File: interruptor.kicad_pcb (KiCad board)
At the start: 2 copper layers, 23 parts, among them J1 220v, J2 tx/rx, J3 Screw_Terminal_01x03, J4 Screw_Terminal_01x03, J5 Int_1, J6 int_2, J7 switch, K1 SRD-05VDC-SL-C, K2 SRD-05VDC-SL-C, Q1 PN2222A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

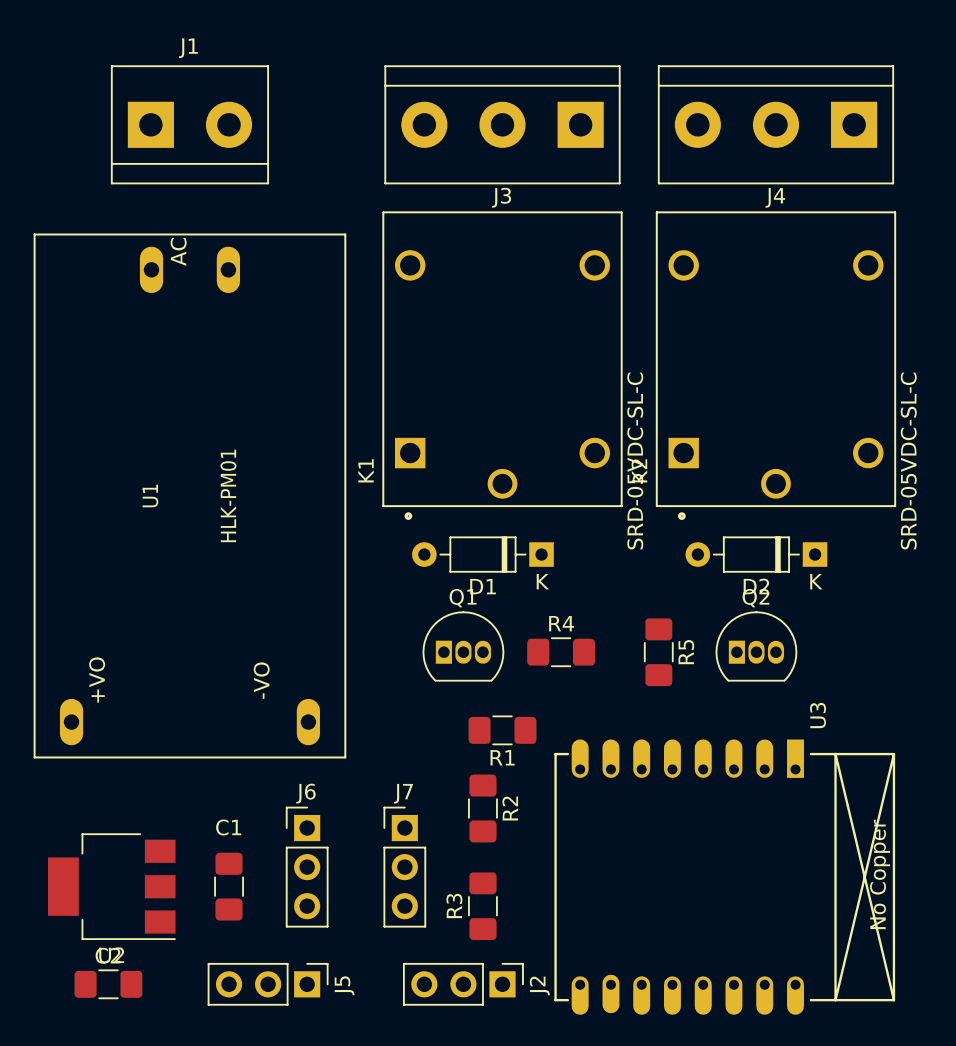
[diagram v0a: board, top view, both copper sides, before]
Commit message: colocacion componentes en pcb y conexionado
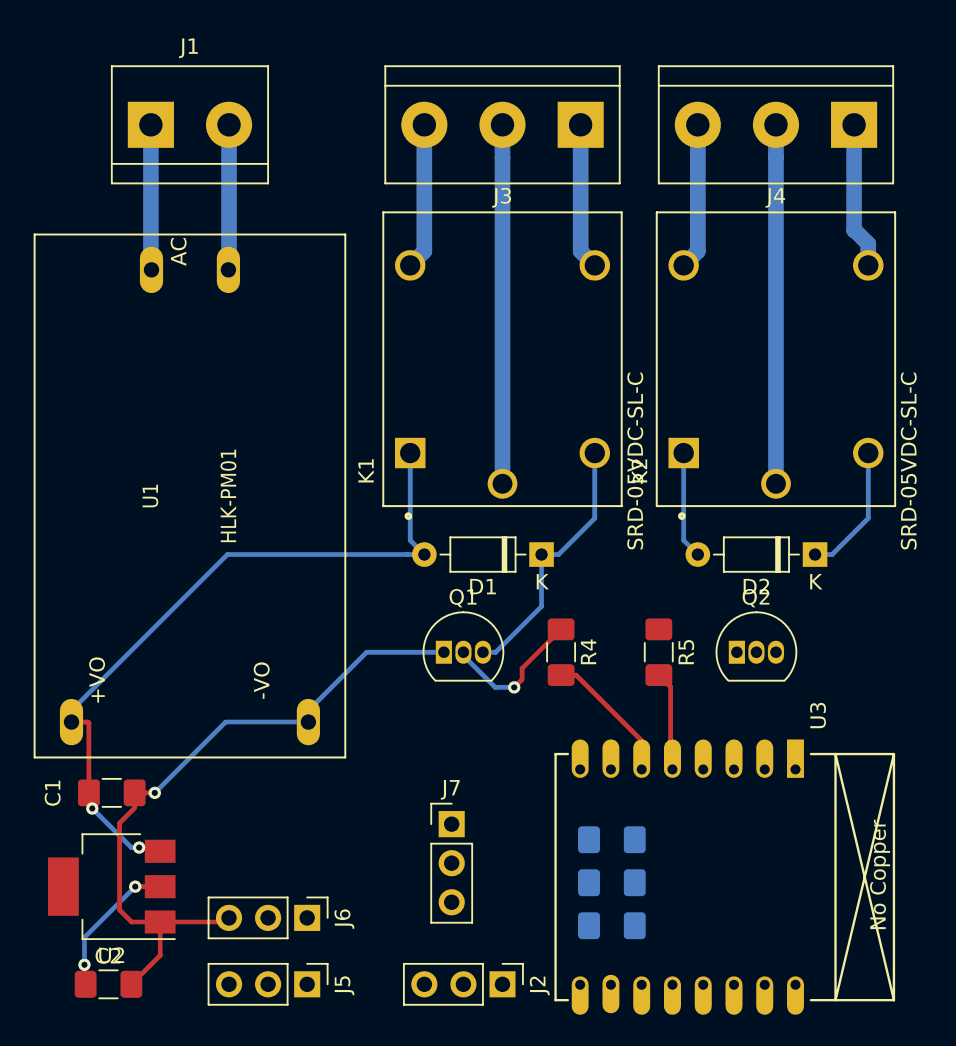
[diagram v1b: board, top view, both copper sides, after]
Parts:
- C1, C2: value 400nF -> 10uF
- R1, R2, R3: moved to B.Cu
- moved R2 11.3 mm to (122.7, 116.8), turned to 180 degrees
- moved R1 10.1 mm to (122.7, 111.3)
- moved C1 9.76 mm to (90.2, 108.2), turned to 0 degrees
- moved R3 8.52 mm to (122.7, 114.0), turned to 0 degrees
- moved J6 5.84 mm to (102.9, 116.3), turned to 270 degrees
- moved J7 3.06 mm to (112.3, 110.2)
- turned R4 to 270 degrees
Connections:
- U3 pad 5: Relay_1 -> Relay_2
- U3 pad 6: Relay_2 -> Relay_1
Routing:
- net Net-(C1-Pad1): track 0.00 -> 54.2 mm, vias 0 -> 2
- net GND: track 0.00 -> 44.7 mm, vias 0 -> 1
- net Net-(J4-Pad2): track 0.00 -> 23.3 mm
- net Net-(J3-Pad2): track 0.00 -> 23.3 mm
- net Net-(D1-Pad1): track 0.00 -> 17.1 mm
- net Net-(J4-Pad1): track 0.00 -> 9.54 mm
- net Net-(J4-Pad3): track 0.00 -> 9.52 mm
- net Net-(J3-Pad3): track 0.00 -> 9.52 mm
- net Net-(J3-Pad1): track 0.00 -> 9.52 mm
- net Net-(J1-Pad2): track 0.00 -> 9.45 mm
- net Net-(J1-Pad1): track 0.00 -> 9.45 mm
- net Net-(Q1-Pad2): track 0.00 -> 9.42 mm, vias 0 -> 1
- net vcc: track 0.00 -> 9.37 mm, vias 0 -> 2
- net Relay_1: track 0.00 -> 8.87 mm
- net Net-(D2-Pad1): track 0.00 -> 8.68 mm
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
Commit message: pistas dibujadas
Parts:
- moved C2 9.04 mm to (97.8, 116.2), turned to 180 degrees
- moved J5 8.19 mm to (103.7, 112.5)
- moved J2 8.05 mm to (115.5, 112.6)
- moved J6 7.53 mm to (103.8, 108.8)
- moved R1 6.91 mm to (123.0, 104.3)
- moved R3 6.83 mm to (123.0, 107.2)
- moved R2 6.50 mm to (123.1, 110.3)
- moved U3 6.44 mm to (134.3, 100.2)
- moved D1 5.74 mm to (112.5, 91.5), turned to 0 degrees
- moved D2 5.59 mm to (130.4, 91.7), turned to 0 degrees
- moved R5 4.38 mm to (127.9, 95.2), turned to 180 degrees
- moved Q2 4.12 mm to (133.2, 95.7)
- moved R4 3.93 mm to (119.8, 95.2), turned to 0 degrees
- moved J7 3.87 mm to (115.7, 108.5), turned to 270 degrees
- moved Q1 3.42 mm to (113.0, 95.8)
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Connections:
- U3 pad 4: int_1 -> Relay_2
- U3 pad 5: Relay_2 -> Relay_1
- U3 pad 6: Relay_1 -> int_1
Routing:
- net GND: track 44.7 -> 91.5 mm, vias 1 -> 2
- net int_1: track 0.00 -> 34.6 mm, vias 0 -> 2
- net vcc: track 9.37 -> 41.6 mm, vias 2 -> 4
- net Net-(J7-Pad2): track 0.00 -> 30.3 mm
- net int_2: track 0.00 -> 27.0 mm
- net Net-(C1-Pad1): track 54.2 -> 79.0 mm
- net Net-(J2-Pad1): track 0.00 -> 19.5 mm
- net Net-(R3-Pad2): track 0.00 -> 13.4 mm, vias 0 -> 1
- net Net-(J2-Pad2): track 0.00 -> 10.8 mm
- net Net-(Q2-Pad2): track 0.00 -> 7.79 mm
- net Net-(R1-Pad1): track 0.00 -> 7.56 mm, vias 0 -> 1
- net Net-(R2-Pad1): track 0.00 -> 4.83 mm, vias 0 -> 1
- net Net-(D1-Pad1): track 17.1 -> 12.4 mm
- net Net-(D2-Pad1): track 8.68 -> 11.5 mm
- net Net-(Q1-Pad2): track 9.42 -> 7.47 mm
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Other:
- board outline added: 56 x 57 mm
- board text added: "Rx"
- board text added: "Tx"
- board text added: "gnd"
- board text added: "int1"
- board text added: "int2"
- board text added: "rec"
- board text added: "vcc"

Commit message: modificadas pistas smd
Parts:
- moved J4 1.83 mm to (136.6, 64.8)
- moved K2 1.35 mm to (132.0, 80.0)
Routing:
- net Relay_1: track 7.67 -> 8.67 mm
- net Net-(D2-Pad1): track 11.5 -> 11.0 mm
- net Net-(C1-Pad1): track 79.0 -> 79.5 mm
- net int_2: track 27.0 -> 27.5 mm
